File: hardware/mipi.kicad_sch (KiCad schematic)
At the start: 20 parts, among them U4 CCGM1A1

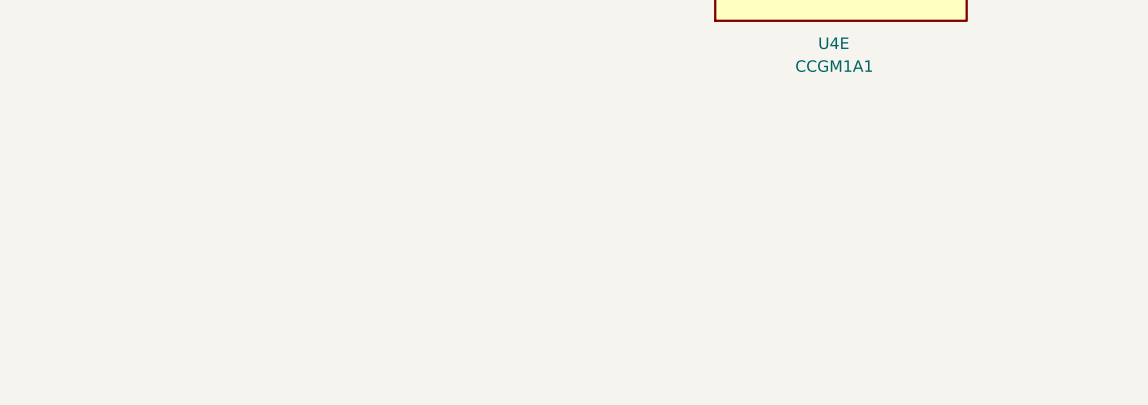
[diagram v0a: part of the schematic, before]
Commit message: Adding USB connector and level converter
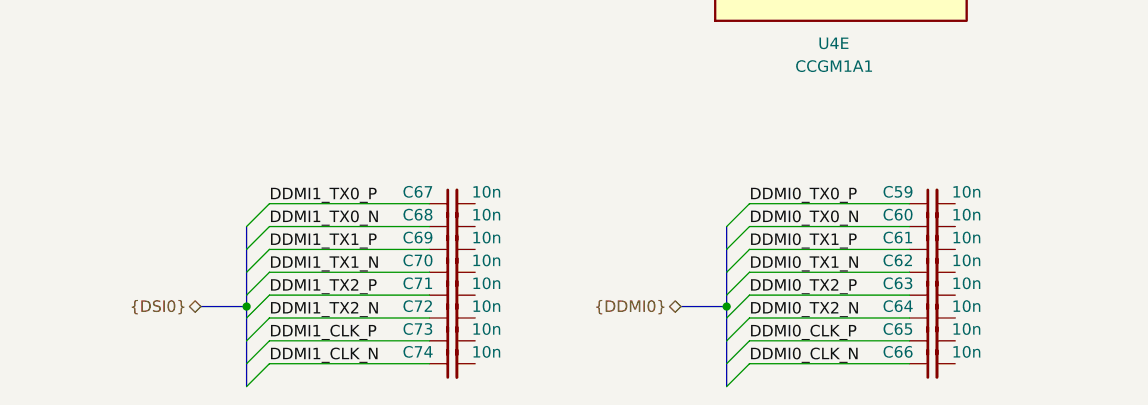
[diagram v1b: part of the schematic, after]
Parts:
- added C59, C60, C61, C62, C63, C64, C65, C66, C67, C68, C69, C70, C71, C72, C73, C74: 10n, Capacitor_SMD:C_0402_1005Metric, symbol Device:C_Small
- U4: footprint Package_BGA:BGA-324_15.0x15.0mm_Layout18x18_P0.8mm_Ball0.45mm_Pad0.4mm_NSMD -> ulx5m-gs:BGA-324_15.0x15.0mm_Layout18x18_P0.8mm_Ball0.45mm_Pad0.4mm_NSMD
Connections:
- new net DDMI0_CLK_N: C66.1
- new net DDMI0_CLK_P: C65.1
- new net DDMI0_TX0_N: C60.1
- new net DDMI0_TX0_P: C59.1
- new net DDMI0_TX1_N: C62.1
- new net DDMI0_TX1_P: C61.1
- new net DDMI0_TX2_N: C64.1
- new net DDMI0_TX2_P: C63.1
- new net DDMI1_CLK_N: C74.1
- new net DDMI1_CLK_P: C73.1
- new net DDMI1_TX0_N: C68.1
- new net DDMI1_TX0_P: C67.1
- new net DDMI1_TX1_N: C70.1
- new net DDMI1_TX1_P: C69.1
- new net DDMI1_TX2_N: C72.1
- new net DDMI1_TX2_P: C71.1

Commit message: Routing diff clock
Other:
- company: (none) -> ${project_creator}
- title: (none) -> ${project_name}
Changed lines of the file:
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@@
 	(generator_version "9.0")
 	(paper "A4")
+	(title_block
+		(title "${project_name}")
+		(date "2025-06-24")
+		(rev "${project_version}")
+		(company "${project_creator}")
+		(comment 1 "${project_license}")
+	)
 	(rectangle
 		(start 207.01 52.07)

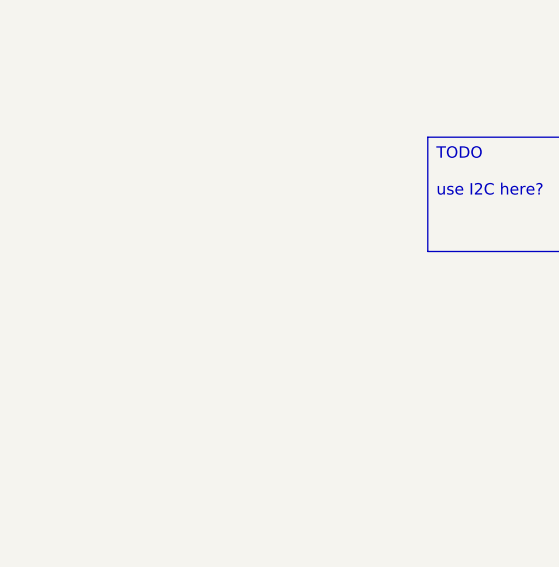
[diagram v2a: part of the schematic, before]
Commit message: Adding LEDs
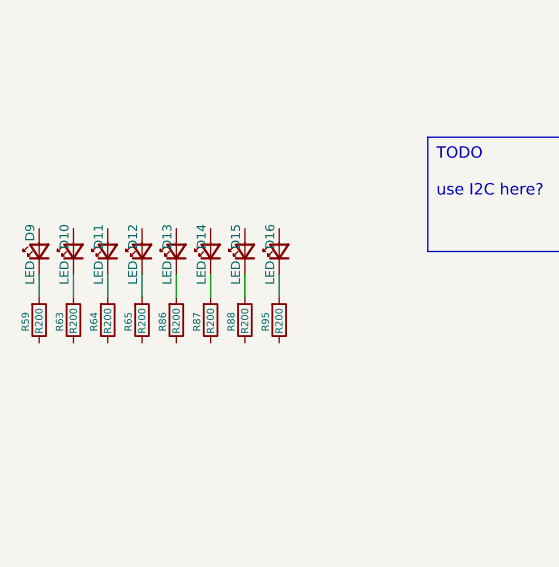
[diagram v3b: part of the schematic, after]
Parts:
- added D10, D11, D12, D13, D14, D15, D16, D9: LED, LED_SMD:LED_0603_1608Metric, symbol Device:LED_Small
- added R59, R63, R64, R65, R86, R87, R88, R95: R200, Resistor_SMD:R_0402_1005Metric, symbol Device:R_Small
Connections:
- new net: D12.1 (K), R65.1
- new net: D10.1 (K), R63.1
- new net: D14.1 (K), R87.1
- new net: D9.1 (K), R59.1
- new net: D11.1 (K), R64.1
- new net: D15.1 (K), R88.1
- new net: D13.1 (K), R86.1
- new net: D16.1 (K), R95.1

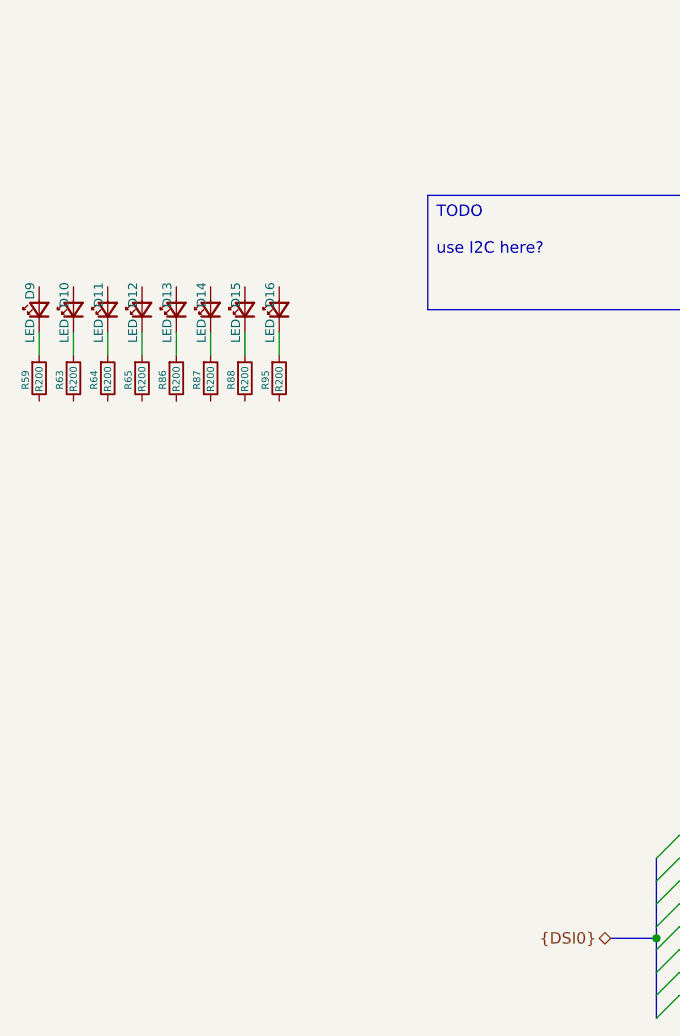
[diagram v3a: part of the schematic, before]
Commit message: Adding Switches and 25MHz oscilator
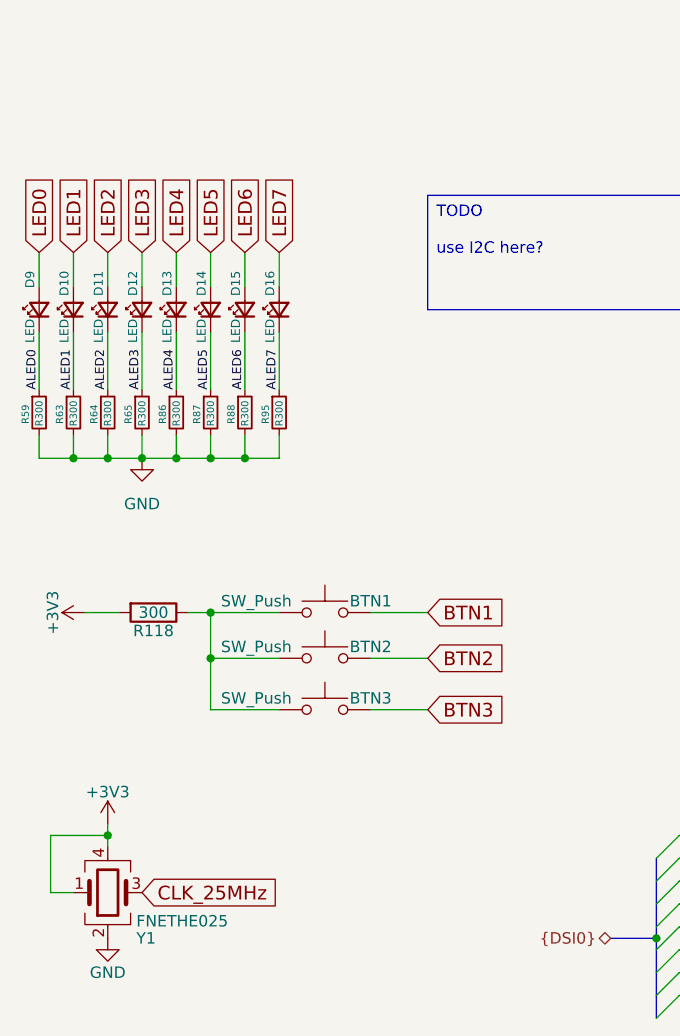
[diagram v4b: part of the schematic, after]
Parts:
- added BTN1, BTN2, BTN3: SW_Push, Switch_EVPAA:Switch_EVPAA, symbol Switch:SW_Push
- added R118: 300, Resistor_SMD:R_0402_1005Metric, symbol Device:R
- added Y1: FNETHE025, Crystal:Crystal_SMD_TXC_7M-4Pin_3.2x2.5mm, symbol Device:Crystal_GND24
- R59, R63, R64, R65, R86, R87, R88, R95: value R200 -> R300
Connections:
- net GND: now also R59.2, R63.2, R64.2, R65.2, R86.2, R87.2, R88.2, R95.2, Y1.2
- net ALED3: now reaches D12.1 (K), R65.1
- net LED3: now reaches D12.2 (A)
- net ALED1: now reaches D10.1 (K), R63.1
- net LED1: now reaches D10.2 (A)
- net ALED5: now reaches D14.1 (K), R87.1
- net ALED0: now reaches D9.1 (K), R59.1
- net LED0: now reaches D9.2 (A)
- net ALED2: now reaches D11.1 (K), R64.1
- net ALED6: now reaches D15.1 (K), R88.1
- net LED2: now reaches D11.2 (A)
- net ALED4: now reaches D13.1 (K), R86.1
- net LED4: now reaches D13.2 (A)
- net LED6: now reaches D15.2 (A)
- net ALED7: now reaches D16.1 (K), R95.1
- net LED7: now reaches D16.2 (A)
- net LED5: now reaches D14.2 (A)
- new net: BTN1.1, BTN2.1, BTN3.1, R118.1
- new net +3V3: R118.2, Y1.1, Y1.4
- new net BTN1: BTN1.2
- new net BTN2: BTN2.2
- new net BTN3: BTN3.2
- new net CLK_25MHz: Y1.3
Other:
- moved on the sheet: R59, R63, R64, R65, R86, R87, R88, R95

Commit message: Clearing errors
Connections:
- net +1V2_SA: now reaches C50.1, C51.1, C52.1, R121.2, U4.P10 (VDD_SA), U4.P6 (VDD_SA), U4.P8 (VDD_SA), U4.U6 (VDD_SA), U4.U9 (VDD_SA)
- net +1V2_SB: now reaches C53.1, C54.1, C55.1, R122.1, U4.N11 (VDD_SB), U4.N13 (VDD_SB), U4.N18 (VDD_SB), U4.R15 (VDD_SB), U4.T18 (VDD_SB)

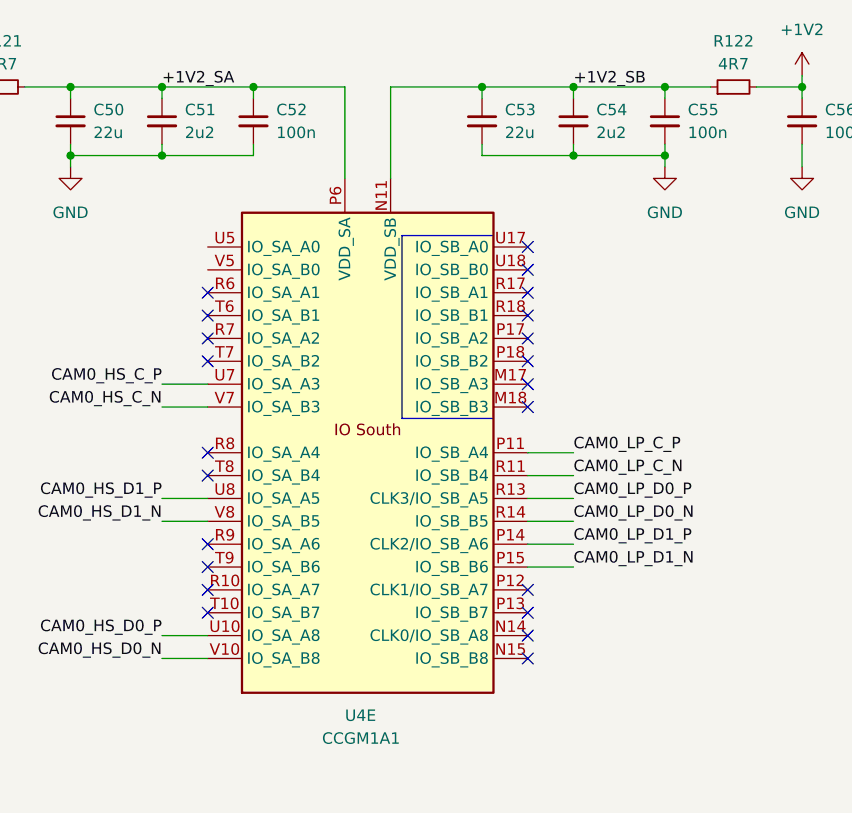
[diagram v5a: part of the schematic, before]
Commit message: Adding more VIAs
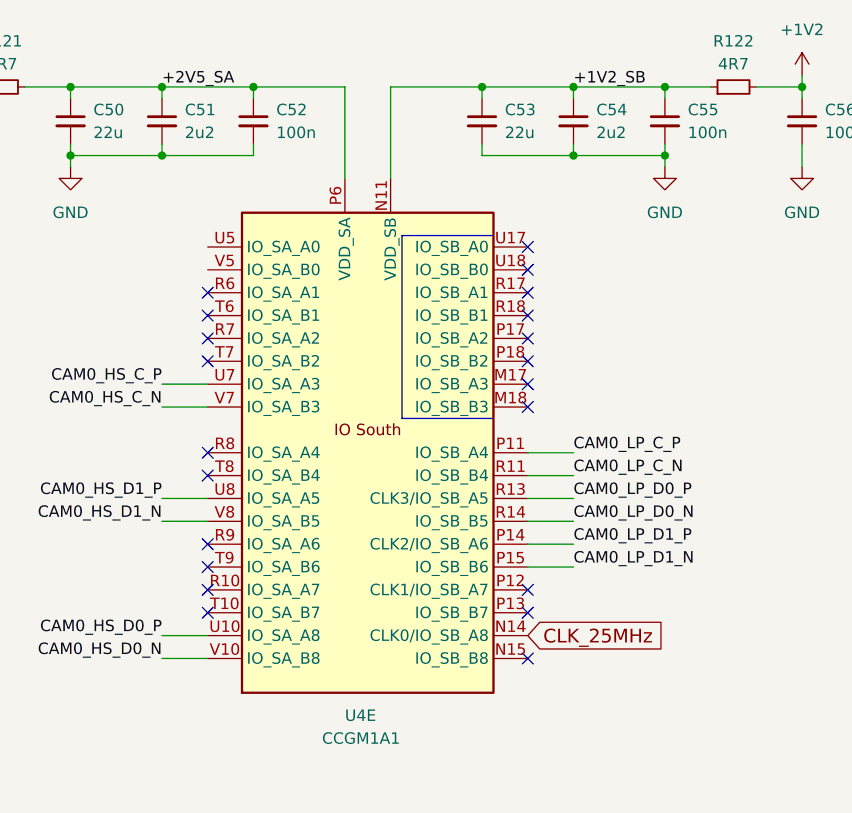
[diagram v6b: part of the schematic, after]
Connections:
- net CLK_25MHz: now also U4.N14 (CLK0/IO_SB_A8)
- net +1V2_SA renamed +2V5_SA
- no-connect marks 22 -> 21
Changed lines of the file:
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@@
-	)
-	(no_connect
-		(at 170.18 99.06)
 	)
 	(no_connect
@@
 		)
 	)
-	(label "+1V2_SA"
+	(label "+2V5_SA"
 		(at 129.54 38.1 0)
 		(effects
@@
 			(effects
 				(font
+					(size 1.27 1.27)
+				)
+				(hide yes)
+			)
+		)
+	)
+	(global_label "CLK_25MHz"
+		(shape input)
+		(at 170.18 99.06 0)
+		(effects
+			(font
+				(size 1.524 1.524)
+			)
+			(justify left)
+		)
+		(property "Intersheetrefs" "${INTERSHEET_REFS}"
+			(at 170.18 99.06 0)
+			(effects
+				(font

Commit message: Updat to CM5
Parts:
- removed BTN1, BTN2, BTN3: SW_Push, Switch_EVPAA:Switch_EVPAA, symbol Switch:SW_Push
- removed C67, C68, C69, C70, C71, C72, C73, C74: 10n, Capacitor_SMD:C_0402_1005Metric, symbol Device:C_Small
- removed R118: 300, Resistor_SMD:R_0402_1005Metric, symbol Device:R
- added R129, R130, R131, R132, R135, R136, R137: 150R, Resistor_SMD:R_0402_1005Metric, symbol Device:R_Small
- R49, R52, R53, R56, R57, R60: now not fitted; now left out of the parts list
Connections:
- net +3V3 is gone; now on net +2V5: Y1.1, Y1.4
- net +1V2: now also C49.1, R121.1; no longer C56.1, R122.2
- net +2V5: now also C56.1, R122.2; no longer C49.1, R121.1
- net CAM0_LP_C_N: no longer U4.R11 (IO_SB_B4)
- net CAM0_LP_C_P: no longer U4.P11 (IO_SB_A4)
- net CAM0_LP_D0_N: no longer U4.R14 (IO_SB_B5)
- net CAM0_LP_D0_P: no longer U4.R13 (CLK3/IO_SB_A5)
- net CAM0_LP_D1_N: no longer U4.P15 (IO_SB_B6)
- net CAM0_LP_D1_P: no longer U4.P14 (CLK2/IO_SB_A6)
- net LED0: now also U4.U17 (IO_SB_A0)
- net LED1: now also U4.U18 (IO_SB_B0)
- net LED2: now also U4.R17 (IO_SB_A1)
- net LED3: now also U4.R18 (IO_SB_B1)
- net LED4: now also U4.P17 (IO_SB_A2)
- net LED5: now also U4.P18 (IO_SB_B2)
- net LED6: now also U4.M17 (IO_SB_A3)
- net LED7: now also U4.M18 (IO_SB_B3)
- net DDMI0_HS_TX2_P: now reaches C63.2
- net DDMI0_HS_TX2_P: now also U4.P14 (CLK2/IO_SB_A6)
- net DDMI0_HS_CLK_P: now reaches C65.2
- net DDMI0_HS_CLK_P: now also U4.P12 (CLK1/IO_SB_A7)
- net DDMI0_HS_TX1_P: now reaches C61.2
- net DDMI0_HS_TX1_P: now also U4.R13 (CLK3/IO_SB_A5)
- net DDMI0_HS_TX0_N: now reaches C60.2
- net DDMI0_HS_TX0_N: now also U4.R11 (IO_SB_B4)
- net DDMI0_HS_TX0_P: now reaches C59.2
- net DDMI0_HS_TX0_P: now also U4.P11 (IO_SB_A4)
- net DDMI0_HS_CLK_N: now reaches U4.P13 (IO_SB_B7)
- net DDMI0_HS_CLK_N: now also C66.2
- net MIPI0_D1_P: now reaches U4.R10 (IO_SA_A7)
- net MIPI0_D1_P: now also R54.1, R57.1
- net MIPI1_C_P: now reaches U4.R6 (IO_SA_A1)
- net MIPI1_C_P: now also R129.1
- net MIPI1_D1_P: now reaches U4.R7 (IO_SA_A2)
- net MIPI1_D1_P: now also R135.1
- net MIPI0_D3_P: now reaches U4.R8 (IO_SA_A4)
- net MIPI0_D3_P: now also R131.1
- net MIPI0_C_P: now reaches U4.R9 (IO_SA_A6)
- net MIPI0_C_P: now also R49.1, R50.1
- net MIPI0_D1_N: now reaches U4.T10 (IO_SA_B7)
- net MIPI0_D1_N: now also R54.2, R60.1
- net MIPI1_C_N: now reaches U4.T6 (IO_SA_B1)
- net MIPI1_C_N: now also R129.2
- net MIPI1_D1_N: now reaches U4.T7 (IO_SA_B2)
- net MIPI1_D1_N: now also R135.2
- net MIPI0_D3_N: now reaches U4.T8 (IO_SA_B4)
- net MIPI0_D3_N: now also R131.2
- net MIPI0_C_N: now reaches U4.T9 (IO_SA_B6)
- net MIPI0_C_N: now also R50.2, R52.1
- net MIPI1_D2_P: now reaches U4.U5 (IO_SA_A0)
- net MIPI1_D2_P: now also R136.1
- net MIPI1_D2_N: now reaches U4.V5 (IO_SA_B0)
- net MIPI1_D2_N: now also R136.2
- net DDMI0_HS_TX2_N: now reaches C64.2
- net DDMI0_HS_TX2_N: now also U4.P15 (IO_SB_B6)
- net DDMI0_HS_TX1_N: now reaches C62.2
- net DDMI0_HS_TX1_N: now also U4.R14 (IO_SB_B5)
- net +1V2_SB renamed +2V5_SB
- net +2V5_SA renamed +1V2_SA
- removed net CAM0_C_N: R50.2, R52.1, U4.V7 (IO_SA_B3)
- removed net CAM0_C_P: R49.1, R50.1, U4.U7 (IO_SA_A3)
- net CAM0_D0_N renamed MIPI0_D0_N
- net CAM0_D0_P renamed MIPI0_D0_P
- removed net CAM0_D1_N: R54.2, R60.1, U4.V8 (IO_SA_B5)
- removed net CAM0_D1_P: R54.1, R57.1, U4.U8 (IO_SA_A5)
- new net MIPI0_D2_N: R130.2, U4.V8 (IO_SA_B5)
- new net MIPI0_D2_P: R130.1, U4.U8 (IO_SA_A5)
- new net MIPI1_D0_N: R132.2, U4.V7 (IO_SA_B3)
- new net MIPI1_D0_P: R132.1, U4.U7 (IO_SA_A3)
- new net MIPI1_D3_N: R137.2
- new net MIPI1_D3_P: R137.1
- no-connect marks 21 -> 0
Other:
- note added: "DDMIO"
- note added: "LEDs"
- moved on the sheet: C56, R50, R51, R54, Y1

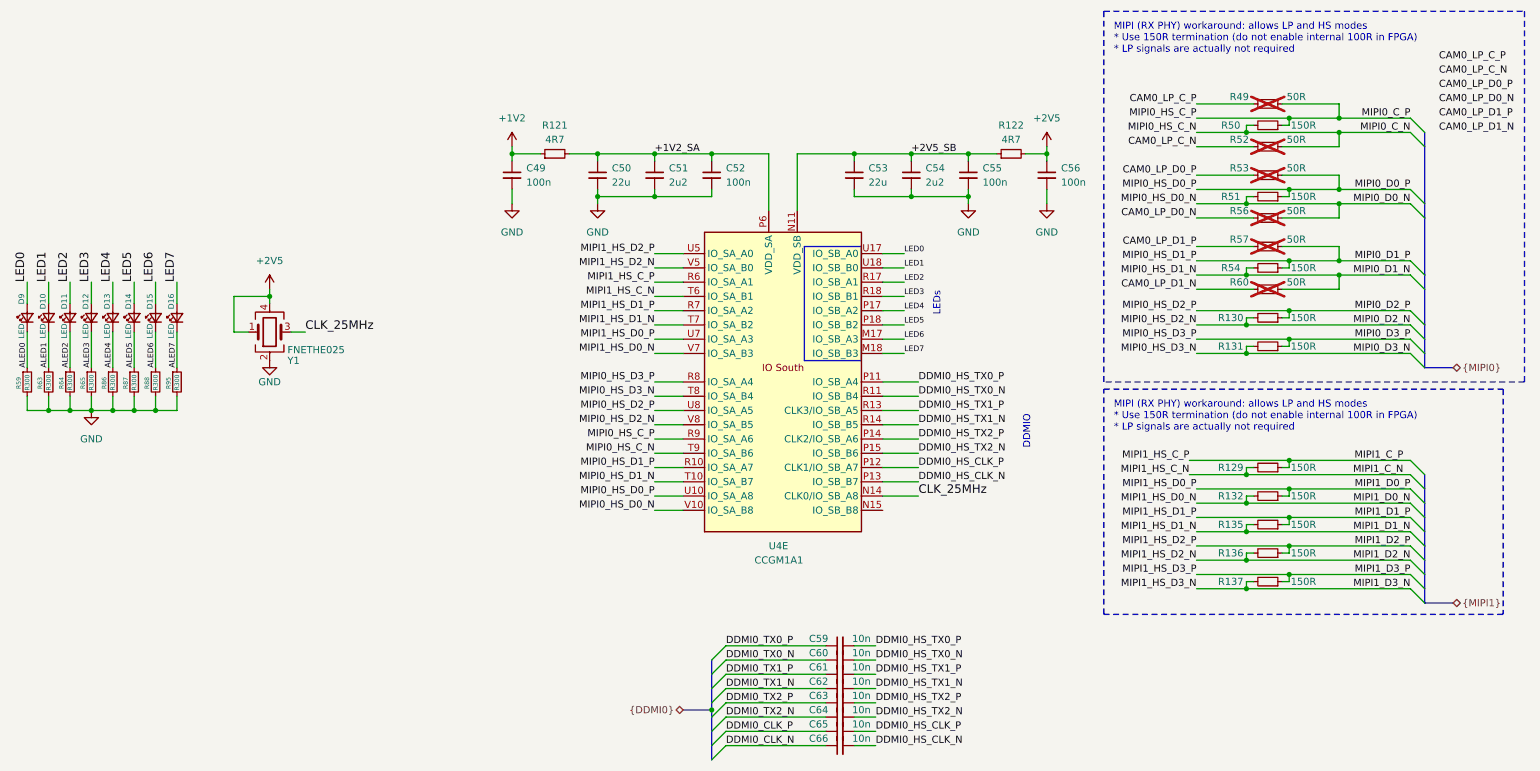
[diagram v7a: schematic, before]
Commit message: Routing GPDI
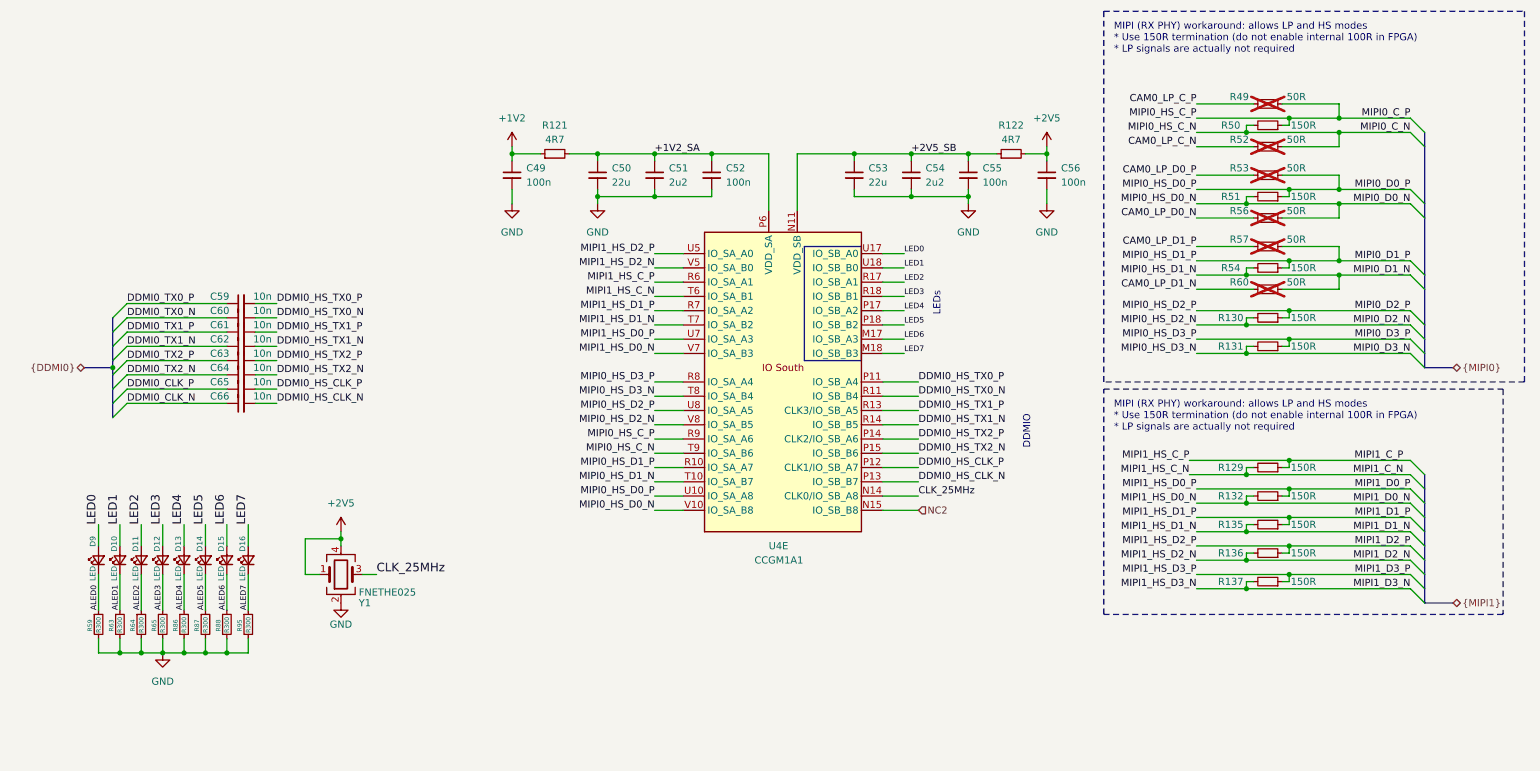
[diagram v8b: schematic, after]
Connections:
- net NC2: now reaches U4.N15 (IO_SB_B8)
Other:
- moved on the sheet: C59, C60, C61, C62, C63, C64, C65, C66, D10, D11, D12, D13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
